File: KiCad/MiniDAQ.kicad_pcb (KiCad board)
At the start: 2 copper layers, 133 parts, among them J1 USB3_A, J2 SMA-J-P-H-ST-EM1, Q1 MMBT3904LP-7B, U1 DS90UB934-Q1, U2 NCP360, U3 SP3010-04UTG, U4 CYUSB3014, U5 M24M02-R, U6 SC189CULTRT, U7 NCP692MN18T2G, Y1 SMD_CRYSTAL

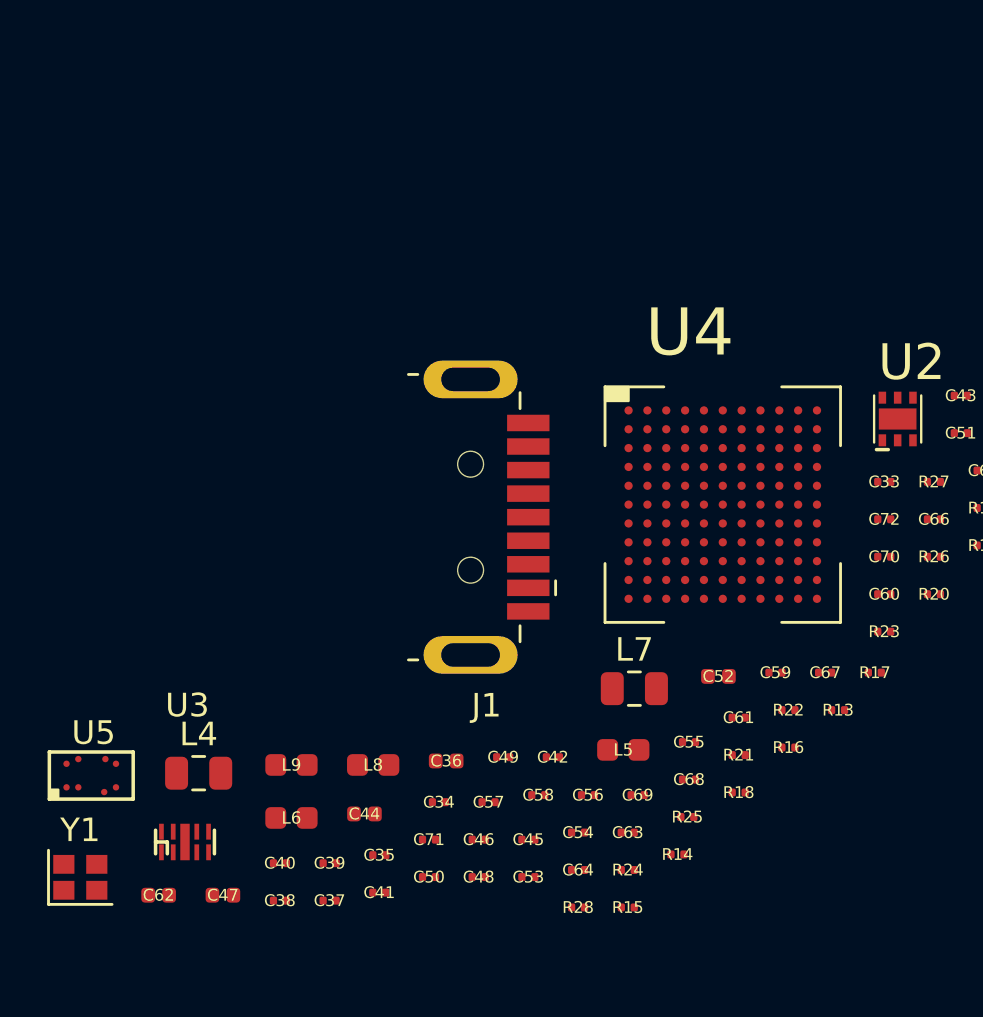
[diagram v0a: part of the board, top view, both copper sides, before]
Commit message: Correct USB to CYUSB3014 connections. I HOPE THIS IS CORRECT!
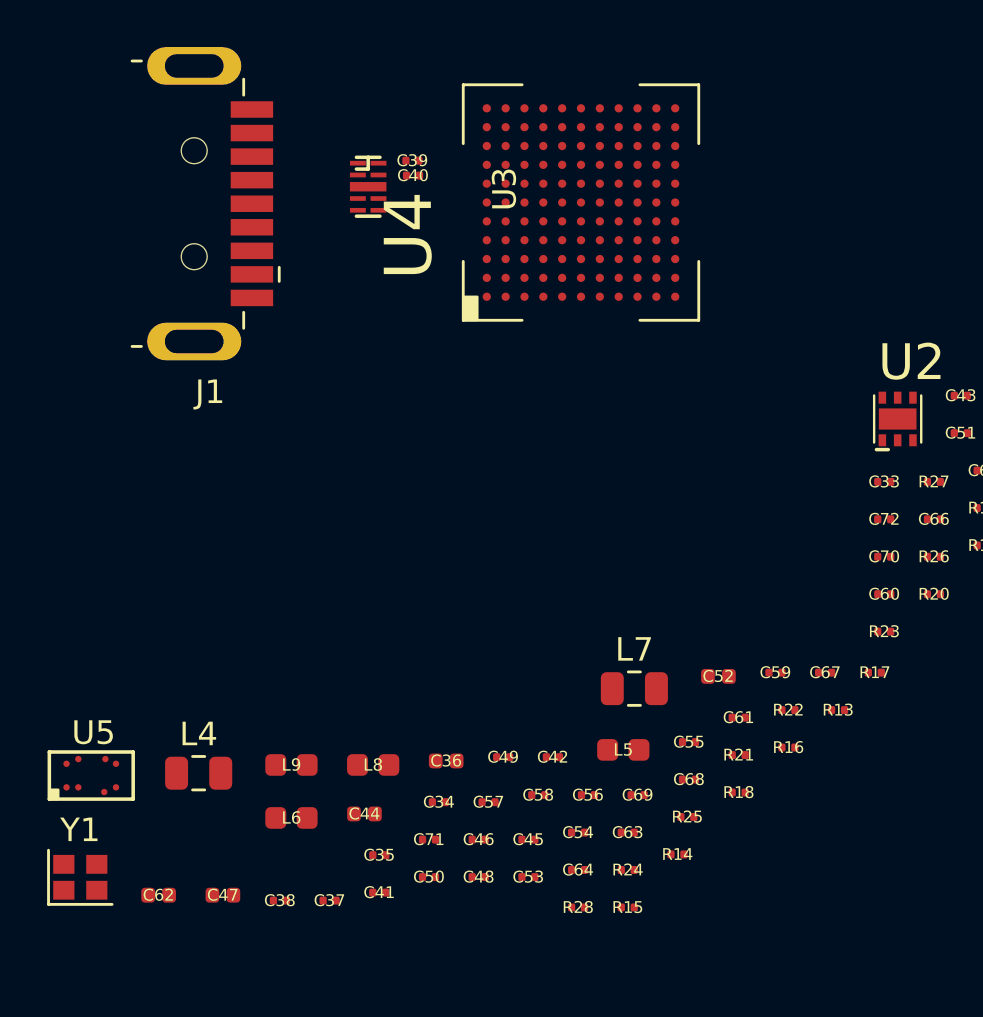
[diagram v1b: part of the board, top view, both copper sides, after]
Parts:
- moved C39 30.0 mm to (90.1, 68.9), turned to 180 degrees
- moved C40 29.7 mm to (90.2, 69.5), turned to 180 degrees
- moved U3 28.9 mm to (88.3, 70.0), turned to 270 degrees
- moved J1 17.7 mm to (81.6, 70.7)
- moved U4 14.2 mm to (97.3, 70.6), turned to 90 degrees
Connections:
- J1 pad 5: /USB/SS_RX_M -> /USB/SS_TX_M
- J1 pad 6: /USB/SS_RX_P -> /USB/SS_TX_P
- J1 pad 8: /USB/SS_TX_M -> /USB/SS_RX_M
- J1 pad 9: /USB/SS_TX_P -> /USB/SS_RX_P
- U4 pad A3: /USB/SS_RX_M -> /USB/SS_RX_P
- U4 pad A4: /USB/SS_RX_P -> /USB/SS_RX_M
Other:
- copper layers 2 -> 6
- net class Default: clearance 0.2 -> 0.1016; trace_width 0.25 -> 0.1016; via_dia 0.8 -> 0.35; via_drill 0.4 -> 0.15
- rule pad_to_mask_clearance: 0.051 -> 0.0254
- rule solder_mask_min_width: 0.25 -> 0.1016
- rule trace_clearance: 0.2 -> 0.1016
- rule trace_min: 0.2 -> 0.1016
- rule via_min_drill: 0.3 -> 0.15
- rule via_min_size: 0.4 -> 0.35

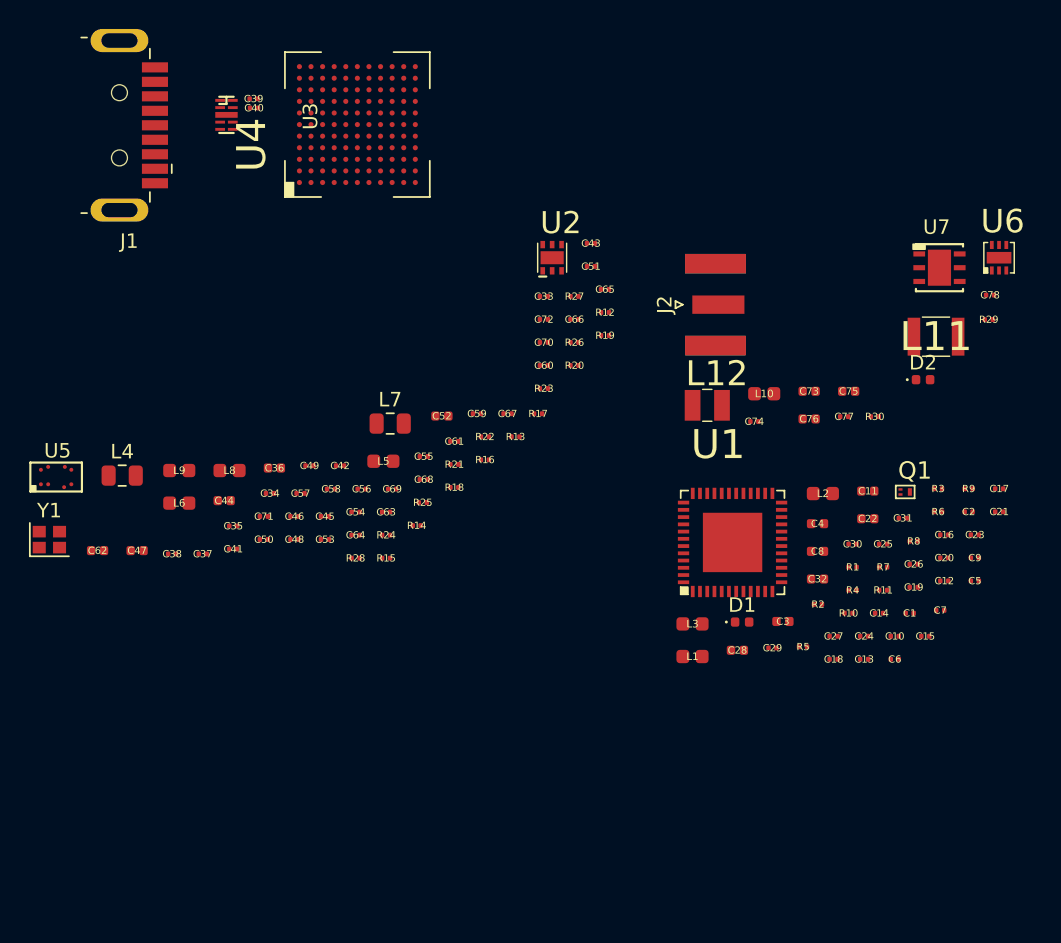
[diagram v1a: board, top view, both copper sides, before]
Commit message: Route PCB. 1.2V and final 5V connection left. Then adding headers
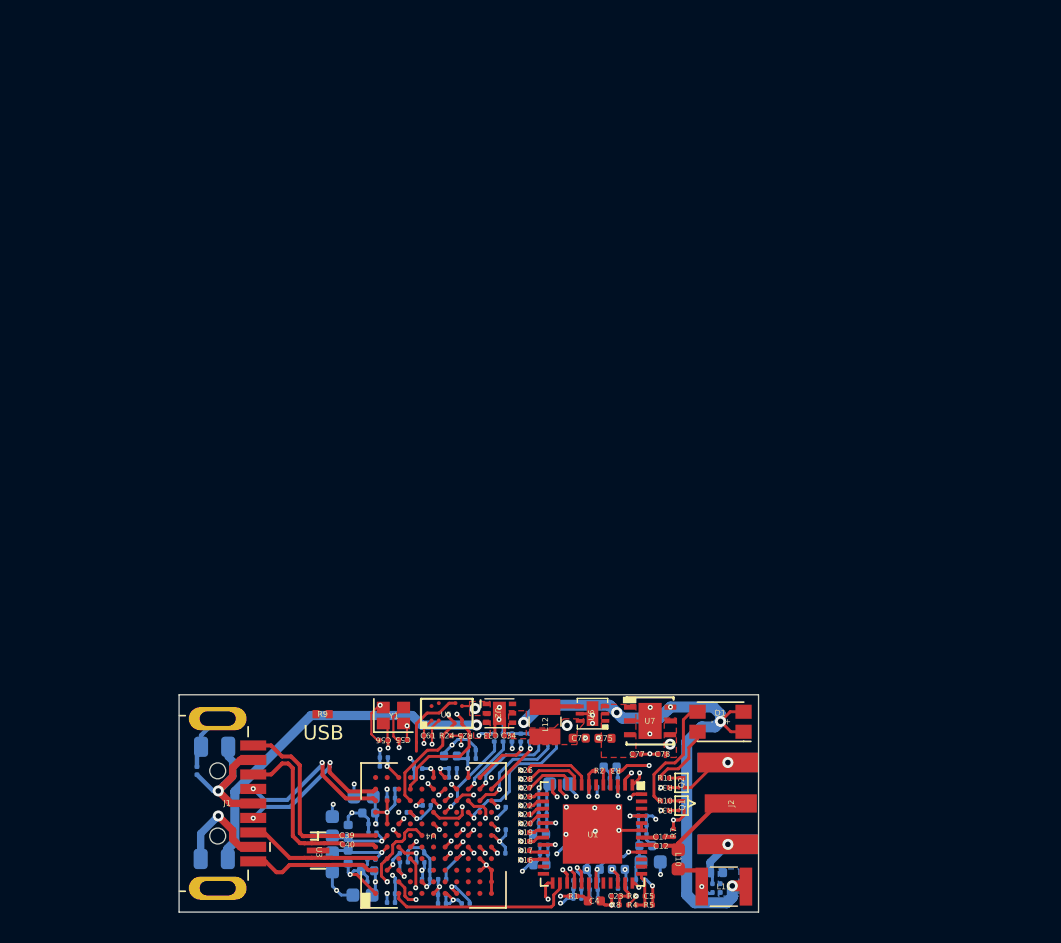
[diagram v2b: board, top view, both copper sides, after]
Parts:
- removed D2: LED_Small_ALT, LED_SMD:LED_0402_1005Metric
- added Q2: MMBT3904LP-7B, .Transistor:TRXDFN3_101X61X53L25X15N, F.Cu at (119.7, 116.1)
- added R31: 2K, .Resistor:R_0201_0603Metric_ERJ_L, F.Cu at (118.5, 118.0)
- added R32: 2K, .Resistor:R_0201_0603Metric_ERJ_L, F.Cu at (118.5, 116.4)
- added R33: 22, .Resistor:R_0201_0603Metric_ERJ_L, B.Cu at (107.4, 113.0)
- added R34: 22, .Resistor:R_0201_0603Metric_ERJ_L, B.Cu at (108.0, 113.0)
- added R35: 22, .Resistor:R_0201_0603Metric_ERJ_L, B.Cu at (108.6, 113.0)
- added R36: 22, .Resistor:R_0201_0603Metric_ERJ_L, B.Cu at (109.2, 113.0)
- added R37: 22, .Resistor:R_0201_0603Metric_ERJ_L, B.Cu at (109.8, 113.0)
- added R38: 22, .Resistor:R_0201_0603Metric_ERJ_L, B.Cu at (110.4, 113.0)
- added R39: 22, .Resistor:R_0201_0603Metric_ERJ_L, B.Cu at (111.0, 113.0)
- added R40: 22, .Resistor:R_0201_0603Metric_ERJ_L, B.Cu at (106.8, 113.0)
- C1, C10, C11, C13, C14, C15, C16, C18, C19, C2, C20, C21, C22, C24, C25, C26, C27, C28, C29, C3, C30, C31, C32, C35, C36, C37, C38, C41, C42, C43, C44, C45, C46, C47, C48, C49, C50, C51, C52, C53, C54, C57, C58, C59, C6, C60, C62, C63, C64, C65, C66, C67, C68, C69, C7, C70, C71, C72, C73, C74, C8, C9, L1, L2, L3, L4, L5, L6, L7, L8, L9, R12, R13, R14, R15, R30: moved to B.Cu
- D1: value LED_Small_ALT -> LTST-C155GEKT; footprint LED_SMD:LED_0402_1005Metric -> .LED:LED_4_P138_270X320X110L50X90N
- R11: value 2K -> 2k
- R29: value 2k -> 10K; moved to B.Cu
- R9: value 50 -> DNL; footprint .Resistor:R_0201_0603Metric_ERJ_L -> .Resistor:R_0402_1005Metric_ERJ_L
- moved R29 54.0 mm to (103.2, 122.7)
- moved C39 51.3 mm to (96.6, 119.7)
- moved C40 51.3 mm to (96.6, 120.3)
- moved U3 51.2 mm to (94.6, 120.8)
- moved U4 49.4 mm to (102.6, 119.7)
- moved J1 47.3 mm to (88.3, 117.5)
- moved R9 47.2 mm to (94.9, 111.3)
- moved C43 46.6 mm to (98.3, 122.9), turned to 180 degrees
- moved U6 42.2 mm to (113.5, 111.3), turned to 90 degrees
- moved C51 41.9 mm to (98.3, 119.5), turned to 180 degrees
- moved L11 40.7 mm to (122.6, 123.2)
- moved C72 40.7 mm to (104.8, 124.4), turned to 180 degrees
- moved R12 39.8 mm to (100.5, 120.9)
- moved C78 38.9 mm to (118.4, 114.1), turned to 180 degrees
- moved U7 37.1 mm to (117.5, 111.8)
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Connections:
- net /USB/SSDM renamed /USB/SSD_N
- net /USB/SSDP renamed /USB/SSD_P
- net /USB/SS_RX_M renamed /USB/SS_RX_N
- net /USB/SS_TX_M renamed /USB/SS_TX_N
- net Net-(C39-Pad1) renamed /USB/TX_N
- net Net-(C40-Pad1) renamed /USB/TX_P
- D1 pad 1: Net-(D1-Pad1) -> +5V
- R10 pad 1: Net-(D1-Pad1) -> Net-(D1-Pad4)
- R11 pad 1: Net-(Q1-Pad1) -> Net-(D1-Pad3)
- R11 pad 2: /Deserializer/LOCK -> Net-(Q2-Pad3)
- R29 pad 1: Net-(D2-Pad1) -> +1V8
- R29 pad 2: GND -> /USB/PMODE1
- R9 pad 1: Net-(R9-Pad1) -> +1V8
- R9 pad 2: GND -> /USB/PMODE0
- U1 pad 25: Net-(U1-Pad25) -> /Deserializer/GPIO3
- U1 pad 26: Net-(U1-Pad26) -> /Deserializer/GPIO2
- U1 pad 27: Net-(U1-Pad27) -> /Deserializer/GPIO1
- U1 pad 28: Net-(U1-Pad28) -> /Deserializer/GPIO0
- U1 pad 38: Net-(R9-Pad1) -> Net-(U1-Pad38)
- U4 pad C1: /USB/SPI_nCS -> /Deserializer/GPIO2
- U4 pad C2: /USB/SPI_MISO -> /Deserializer/GPIO3
- U4 pad D4: /USB/SPI_SCK -> /Deserializer/GPIO0
- U4 pad D5: /USB/SPI_MOSI -> /Deserializer/GPIO1
- U4 pad G5: Net-(U4-PadG5) -> /USB/STATUS
- U4 pad G8: +1V8 -> Net-(R40-Pad2)
- U4 pad H6: Net-(U4-PadH6) -> /USB/LOCK_OUT
- U4 pad J10: GND -> Net-(R33-Pad2)
- U4 pad J8: GND -> Net-(R39-Pad2)
- U4 pad J9: GND -> Net-(R34-Pad2)
- U4 pad K10: GND -> Net-(R37-Pad2)
- U4 pad K11: GND -> Net-(R35-Pad2)
- U4 pad K5: Net-(U4-PadK5) -> /Deserializer/LOCK
- U4 pad K9: GND -> Net-(R38-Pad2)
- U4 pad L10: GND -> Net-(R36-Pad2)
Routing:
- net GND: track 0.00 -> 107.2 mm, vias 0 -> 47
- net +5V: track 0.00 -> 38.0 mm, vias 0 -> 6
- net +1V8: track 0.00 -> 25.7 mm, vias 0 -> 18
- net /Deserializer/I2C_SDA: track 0.00 -> 24.3 mm, vias 0 -> 2
- net Net-(C33-Pad1): track 0.00 -> 24.0 mm, vias 0 -> 1
- net /Deserializer/I2C_SCL: track 0.00 -> 23.7 mm, vias 0 -> 2
- net /USB/LOCK_OUT: track 0.00 -> 19.8 mm, vias 0 -> 2
- net /USB/STATUS: track 0.00 -> 19.5 mm, vias 0 -> 2
- net /Deserializer/VDD18: track 0.00 -> 15.9 mm, vias 0 -> 2
- net /Deserializer/GPIO0: track 0.00 -> 14.9 mm, vias 0 -> 2
- net +1V2: track 0.00 -> 14.5 mm, vias 0 -> 11
- net /Deserializer/LOCK: track 0.00 -> 13.8 mm, vias 0 -> 2
- net /Deserializer/GPIO1: track 0.00 -> 13.5 mm, vias 0 -> 2
- net /Deserializer/GPIO3: track 0.00 -> 13.2 mm, vias 0 -> 2
- net /Deserializer/GPIO2: track 0.00 -> 13.0 mm
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- added copper zone on F.Cu, net +1V2
- added copper zone on F.Cu, net +1V8
- added copper zone on In4.Cu, net +1V8
- added copper zone on B.Cu, net +5V
- added copper zone on F.Cu, net +5V
- added copper zone on F.Cu, net GND
- added copper zone on In1.Cu, net GND
- added copper zone on F.Cu, net Net-(C33-Pad1)
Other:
- board outline added: 40 x 15 mm
- board text added: "Maybe put UART header"
- board text added: "Maybe put header"
- board text added: "USB"

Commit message: All files for v0.1 fab and assembly through PCBway
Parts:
- added C79: 0 Res, .Capacitor:C_0201_0603Metric_L, B.Cu at (115.6, 124.0)
- added G***: LOGO, .Logo:Miniscope_Logo5, B.Cu at (91.9, 117.6)
- added J3: Conn_01x01, .Connector:Conn_1x1_700_Circular_Pad, B.Cu at (110.7, 115.0)
- added J4: Conn_01x01, .Connector:Conn_1x1_700_Circular_Pad, B.Cu at (111.9, 115.0)
- added J5: Conn_01x01, .Connector:Conn_1x1_700_Circular_Pad, B.Cu at (113.3, 115.0)
- added J6: Conn_01x01, .Connector:Conn_1x1_700_Circular_Pad, B.Cu at (111.9, 113.8)
- added J7: Conn_01x03, Connector_PinHeader_1.27mm:PinHeader_1x03_P1.27mm_Vertical, F.Cu at (91.3, 123.6)
- added JP1: Jumper_2_Open, Connector_PinHeader_1.27mm:PinHeader_1x02_P1.27mm_Vertical, F.Cu at (92.6, 111.4)
- added R41: 0, .Resistor:R_0201_0603Metric_ERJ_L, B.Cu at (115.0, 117.0)
- added R42: 0, .Resistor:R_0201_0603Metric_ERJ_L, B.Cu at (110.1, 122.5)
- added R43: 10K, .Resistor:R_0201_0603Metric_ERJ_L, F.Cu at (94.4, 110.6)
- R14: value 22 -> 10K
- R4: value 25.5K 1% -> 10K 1%
- R5: value 95.3K 1% -> 0 1%
- R6: value ???? -> 10K 1%
- R8: value ????? -> 0 1%
- R9: value DNL -> 10K; footprint .Resistor:R_0402_1005Metric_ERJ_L -> .Resistor:R_0201_0603Metric_ERJ_L; moved to B.Cu
- moved R9 24.6 mm to (115.6, 124.5)
- moved C35 0.05 mm to (98.3, 118.9)
- moved C51 0.05 mm to (98.3, 119.5)
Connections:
- R9 pad 1: +1V8 -> /Deserializer/VDD11_FPD
- R9 pad 2: /USB/PMODE0 -> +1V8
- U4 pad K6: Net-(U4-PadK6) -> /USB/GPIO2
- U4 pad K7: Net-(U4-PadK7) -> /USB/GPIO1
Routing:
- net +1V2: track 14.5 -> 36.4 mm, vias 11 -> 13
- net /USB/GPIO1: track 0.00 -> 20.7 mm, vias 0 -> 2
- net /USB/GPIO2: track 0.00 -> 18.1 mm, vias 0 -> 2
- net /USB/PMODE0: track 0.53 -> 16.8 mm, vias 1 -> 2
- net +5V: track 38.0 -> 45.8 mm
- net +1V8: track 25.7 -> 33.1 mm, vias 18 -> 20
- net GND: track 107.2 -> 113.8 mm, vias 47 -> 49
- net /Deserializer/ROUT11: track 1.00 -> 4.73 mm
- net Net-(JP1-Pad2): track 0.00 -> 3.22 mm
- net /Deserializer/ROUT10: track 0.95 -> 3.27 mm
- net /Deserializer/VDD11_FPD: track 2.60 -> 3.82 mm
- net /Deserializer/PCLK: track 4.76 -> 5.70 mm, vias 0 -> 1
- net /Deserializer/VDD11_DVP: track 2.76 -> 3.54 mm
- net Net-(L10-Pad2): track 3.68 -> 4.36 mm
- added copper zone on In2.Cu, net +1V2
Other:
- board text added: "D15"
- board text added: "D8"
- board text added: "GND"
- board text added: "MiniDAQ"
- board text added: "PCLK"
- board text added: "USB Boot"
- board text added: "v0.1"
- board text removed: "Maybe put UART header"
- board text removed: "Maybe put header"
- board text removed: "USB"

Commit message: Minor changes and added test pads for possible v1.0 of MiniDAQ
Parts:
- added J_NA: Conn_01x01, .Connector:Conn_1x1_700_Circular_Pad, F.Cu at (112.4, 114.0)
- added J_NA: Conn_01x01, .Connector:Conn_1x1_700_Circular_Pad, F.Cu at (113.6, 114.0)
- added J_NA: Conn_01x01, .Connector:Conn_1x1_700_Circular_Pad, F.Cu at (111.1, 114.0)
- added J_NA: Conn_01x01, .Connector:Conn_1x1_700_Circular_Pad, F.Cu at (109.8, 114.0)
- added J_NA: Conn_01x01, .Connector:Conn_1x1_700_Circular_Pad, F.Cu at (108.8, 124.0)
- added J_NA: Conn_01x01, .Connector:Conn_1x1_700_Circular_Pad, F.Cu at (108.8, 123.0)
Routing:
- net +5V: track 45.8 -> 51.5 mm
- net +1V8: track 33.1 -> 36.2 mm
- net /Deserializer/ROUT0: track 0.00 -> 2.41 mm
- net /Deserializer/ROUT1: track 0.00 -> 1.94 mm
- net +1V2: track 36.4 -> 37.7 mm
- net GND: track 113.8 -> 114.6 mm
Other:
- board text added: "0"
- board text added: "1"
- board text added: "1.2V"
- board text added: "1.8V"
- board text added: "10"
- board text added: "11"
- board text added: "5V"
- board text added: "v1.0"
- board text removed: "v0.1"

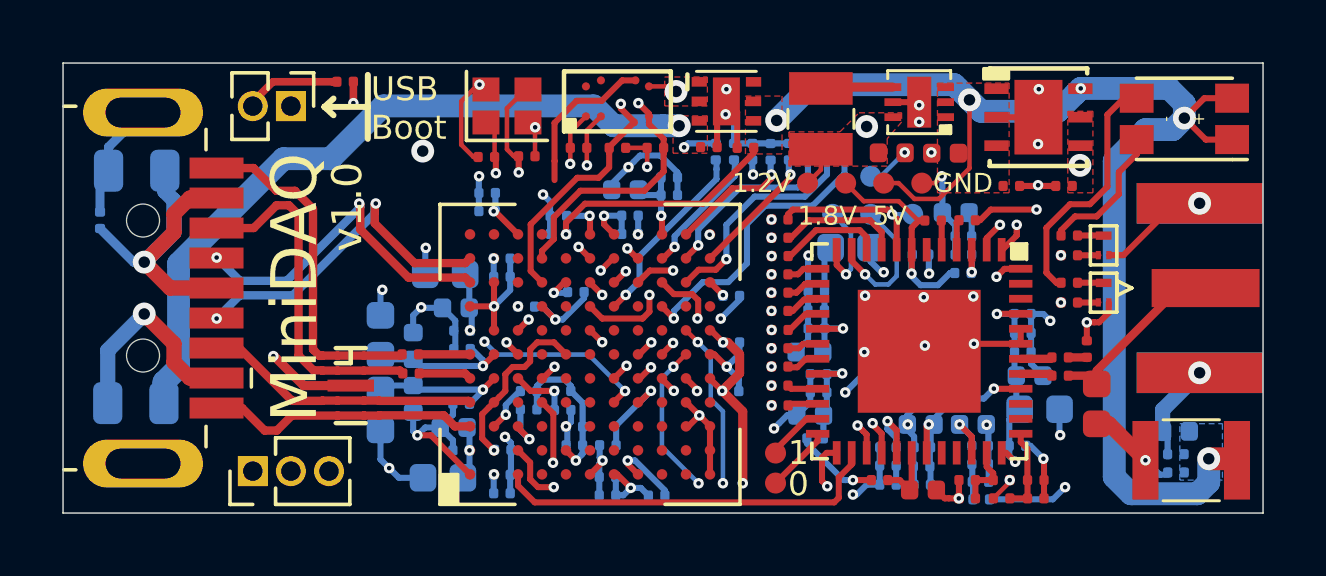
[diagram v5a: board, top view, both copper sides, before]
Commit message: Update v1.0 gerbers and generate .step file.
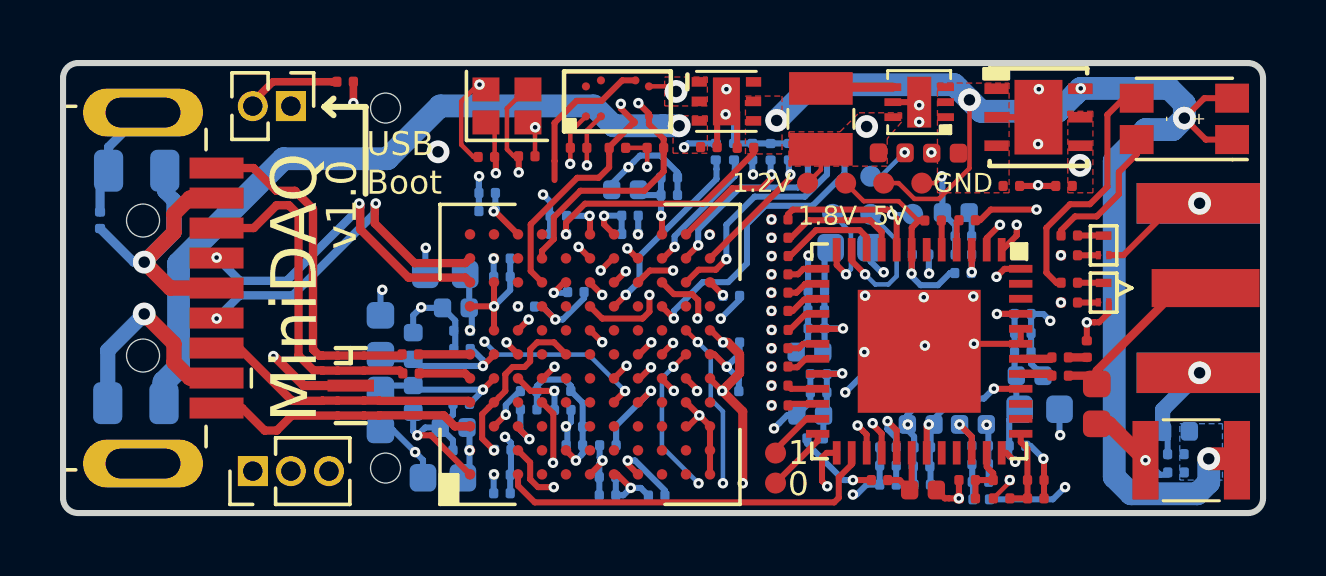
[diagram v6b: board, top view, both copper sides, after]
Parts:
- added J_NA: Conn_01x01, .Connector:Conn_1x1_700_Circular_Pad, F.Cu at (95.8, 111.5)
- added J_NA: Conn_01x01, .Connector:Conn_1x1_700_Circular_Pad, F.Cu at (95.8, 123.5)
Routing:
- net +1V2: track 37.7 -> 36.9 mm
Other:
- outline, holes or cut-outs redrawn
